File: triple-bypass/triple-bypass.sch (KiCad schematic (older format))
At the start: 65 parts, among them CON101 MD-90SM, J101 HDR1X2, J102 HDR1X3, U101 THS7374IPWR, U102 LMV358M8G-13

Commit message: more parts placement
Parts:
- renumbered SL2 to SR2, XL2 to XR2, YL2 to YR2
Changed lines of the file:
@@
 $EndDescr
 $Comp
-L +5V #PWR01
+L +5V #PWR9
 U 1 1 5A68CA11
 P 9000 1050
-F 0 "#PWR01" H 9000 900 50  0001 C CNN
+F 0 "#PWR9" H 9000 900 50  0001 C CNN
 F 1 "+5V" H 9000 1190 50  0000 C CNN
 F 2 "" H 9000 1050 50  0001 C CNN
@@
 $EndComp
 $Comp
-L GND #PWR02
+L GND #PWR10
 U 1 1 5A68CAEB
 P 9000 2650
-F 0 "#PWR02" H 9000 2400 50  0001 C CNN
+F 0 "#PWR10" H 9000 2400 50  0001 C CNN
 F 1 "GND" H 9000 2500 50  0000 C CNN
 F 2 "" H 9000 2650 50  0001 C CNN
@@
 $EndComp
 $Comp
-L GND #PWR03
+L GND #PWR3
 U 1 1 5A68EF32
 P 2650 2900
-F 0 "#PWR03" H 2650 2650 50  0001 C CNN
+F 0 "#PWR3" H 2650 2650 50  0001 C CNN
 F 1 "GND" H 2650 2750 50  0000 C CNN
 F 2 "" H 2650 2900 50  0001 C CNN
@@
 $EndComp
 $Comp
-L +5V #PWR04
+L +5V #PWR5
 U 1 1 5A68FF2A
 P 3700 2300
-F 0 "#PWR04" H 3700 2150 50  0001 C CNN
+F 0 "#PWR5" H 3700 2150 50  0001 C CNN
 F 1 "+5V" H 3700 2440 50  0000 C CNN
 F 2 "" H 3700 2300 50  0001 C CNN
@@
 $EndComp
 $Comp
-L +5V #PWR05
+L +5V #PWR1
 U 1 1 5A693A27
 P 1650 850
-F 0 "#PWR05" H 1650 700 50  0001 C CNN
+F 0 "#PWR1" H 1650 700 50  0001 C CNN
 F 1 "+5V" H 1650 990 50  0000 C CNN
 F 2 "" H 1650 850 50  0001 C CNN
@@
 CSYNC at video level \nalways drives the CVBS \nsignal because bags of\nmoney from HD Retrovision
 $Comp
-L GND #PWR06
+L GND #PWR8
 U 1 1 5A6ACD1A
 P 8025 6200
-F 0 "#PWR06" H 8025 5950 50  0001 C CNN
+F 0 "#PWR8" H 8025 5950 50  0001 C CNN
 F 1 "GND" H 8025 6050 50  0000 C CNN
 F 2 "" H 8025 6200 50  0001 C CNN
@@
 $EndComp
 $Comp
-L +5V #PWR07
+L +5V #PWR7
 U 1 1 5A6ADA07
 P 8025 5150
-F 0 "#PWR07" H 8025 5000 50  0001 C CNN
+F 0 "#PWR7" H 8025 5000 50  0001 C CNN
 F 1 "+5V" H 8025 5290 50  0000 C CNN
 F 2 "" H 8025 5150 50  0001 C CNN
@@
 $EndComp
 $Comp
-L +5V #PWR08
+L +5V #PWR4
 U 1 1 5A6B0DB3
 P 2975 7275
-F 0 "#PWR08" H 2975 7125 50  0001 C CNN
+F 0 "#PWR4" H 2975 7125 50  0001 C CNN
 F 1 "+5V" H 2975 7415 50  0000 C CNN
 F 2 "" H 2975 7275 50  0001 C CNN
@@
 $EndComp
 $Comp
-L GND #PWR09
+L GND #PWR6
 U 1 1 5A6B0E82
 P 4175 7400
-F 0 "#PWR09" H 4175 7150 50  0001 C CNN
+F 0 "#PWR6" H 4175 7150 50  0001 C CNN
 F 1 "GND" H 4175 7250 50  0000 C CNN
 F 2 "" H 4175 7400 50  0001 C CNN
@@
 $EndComp
 $Comp
-L GND #PWR010
+L GND #PWR2
 U 1 1 5A6C4582
 P 2000 6800
-F 0 "#PWR010" H 2000 6550 50  0001 C CNN
+F 0 "#PWR2" H 2000 6550 50  0001 C CNN
 F 1 "GND" H 2000 6650 50  0000 C CNN
 F 2 "" H 2000 6800 50  0001 C CNN
@@
 Connection ~ 2000 5200
 $Comp
-L TP_50 XL2
+L TP_50 XR2
 U 1 1 5A6CEA61
 P 1150 5600
-F 0 "XL2" H 825 5600 60  0000 C CNN
+F 0 "XR2" H 825 5600 60  0000 C CNN
 F 1 "TP_50" H 1250 5800 60  0001 C CNN
 F 2 "db-smt:TP50" H 1450 5900 60  0001 C CNN
@@
 $EndComp
 $Comp
-L TP_50 SL2
+L TP_50 SR2
 U 1 1 5A6CEB6B
 P 1150 6000
-F 0 "SL2" H 825 6000 60  0000 C CNN
+F 0 "SR2" H 825 6000 60  0000 C CNN
 F 1 "TP_50" H 1250 6200 60  0001 C CNN
 F 2 "db-smt:TP50" H 1450 6300 60  0001 C CNN
@@
 $EndComp
 $Comp
-L TP_50 YL2
+L TP_50 YR2
 U 1 1 5A6CEC64
 P 1150 6400
-F 0 "YL2" H 825 6400 60  0000 C CNN
+F 0 "YR2" H 825 6400 60  0000 C CNN
 F 1 "TP_50" H 1250 6600 60  0001 C CNN
 F 2 "db-smt:TP50" H 1450 6700 60  0001 C CNN

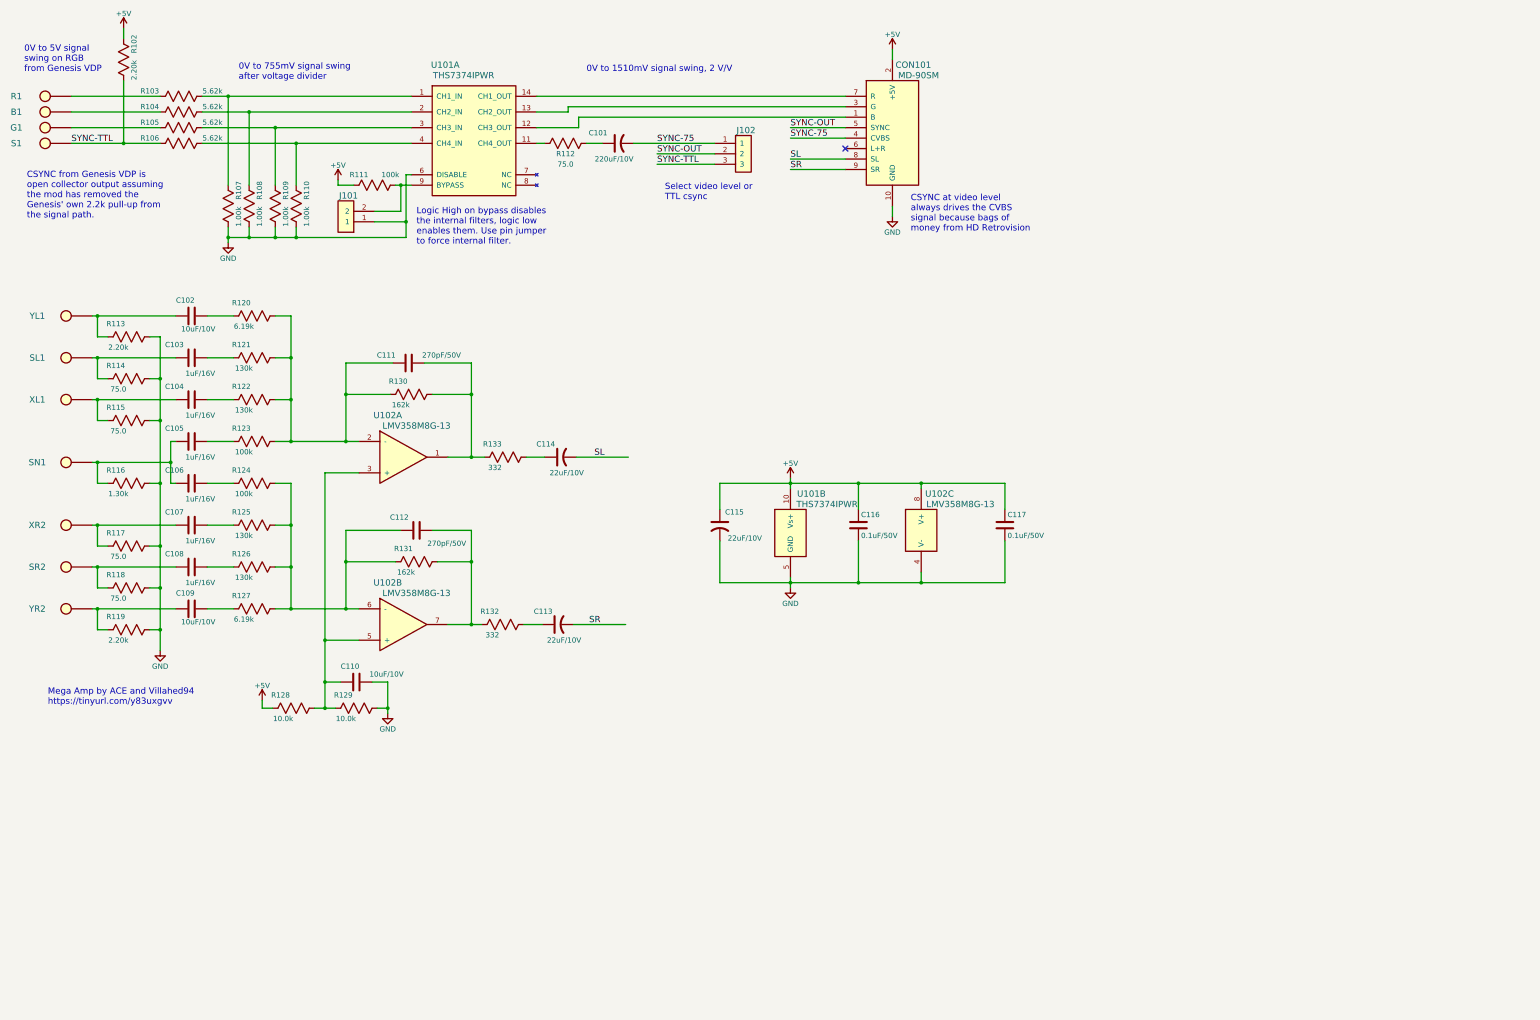
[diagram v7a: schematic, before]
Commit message: v0.3 prelim routing complete, sch added
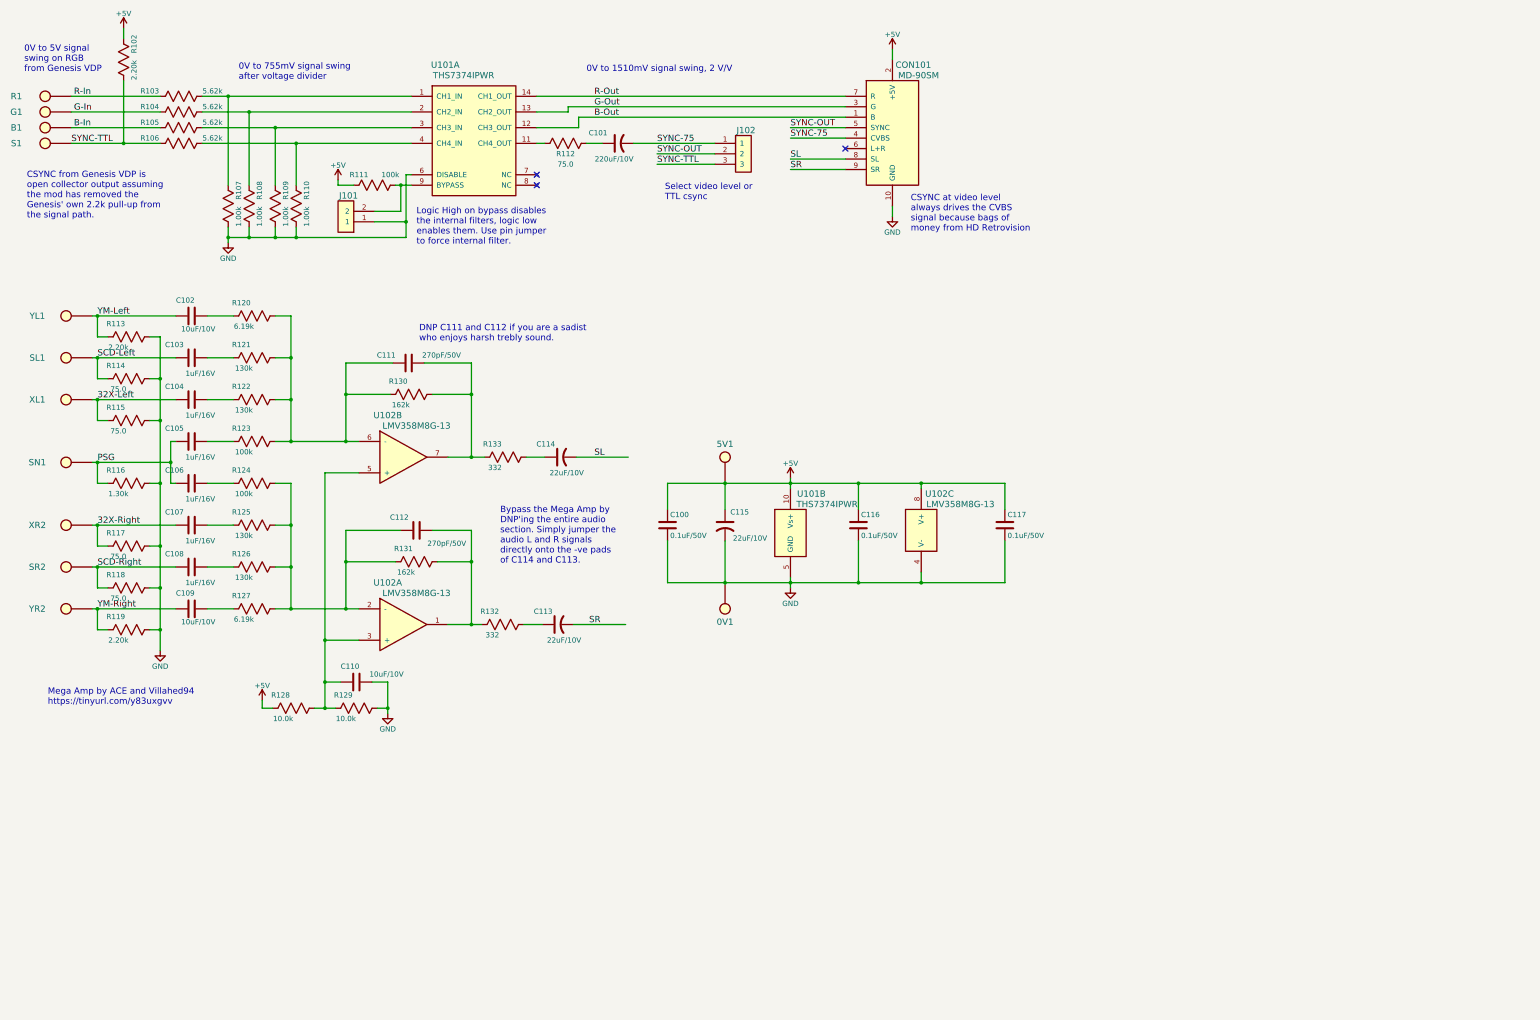
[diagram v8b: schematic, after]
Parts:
- added 0V1, 5V1: TP_50, db-smt:TP50, symbol TP_50
- added C100: 0.1uF/50V, db-smt:0603, symbol C
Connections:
- net +5V: now also 5V1.1, C100.1
- net GND: now also 0V1.1, C100.2
- net B-In: now reaches R105.2
- net B-In: now also B1.1; no longer G1.1
- net G-In: now reaches R104.2
- net G-In: now also G1.1; no longer B1.1
- net R-In: now reaches R1.1, R103.2
- net at C111.2, R130.2, R133.1: now also U102.7 (OUTB); no longer U102.1 (OUTA)
- net at C111.1, R120.2, R121.2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: now also U102.6 (-); no longer U102.2 (-)
- net at C112.1, R124.2, R125.2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: now also U102.2 (-); no longer U102.6 (-)
- net at C112.2, R131.2, R132.1: now also U102.1 (OUTA); no longer U102.7 (OUTB)
- net B-Out: now reaches CON101.1 (B), U101.12 (CH3_OUT)
- net G-Out: now reaches CON101.3 (G), U101.13 (CH2_OUT)
- net R-Out: now reaches CON101.7 (R), U101.14 (CH1_OUT)
- net YM-Left: now reaches C102.2, R113.1, YL1.1
- net SCD-Left: now reaches C103.1, R114.1, SL1.1
- net 32X-Left: now reaches C104.1, R115.1, XL1.1
- net PSG: now reaches C105.1, C106.1, R116.1, SN1.1
- net 32X-Right: now reaches C107.1, R117.1, XR2.1
- net SCD-Right: now reaches C108.1, R118.1, SR2.1
- net YM-Right: now reaches C109.2, R119.1, YR2.1
- no-connect marks 1 -> 3
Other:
- note added: "Bypass the Mega Amp by \nDNP'ing the entire audio \nsection. Simply jumper the\naudio L and R signals \ndirectly onto the -ve pads \nof C114 and C113."
- note added: "DNP C111 and C112 if you are a sadist \nwho enjoys harsh trebly sound."
- moved on the sheet: B1, C115, G1, U102A, U102B
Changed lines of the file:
@@
 Sheet 1 1
 Title "Triple Bypass"
-Date "2018-01-25"
-Rev "0.2"
+Date "2018-08-01"
+Rev "0.3"
 Comp "db Electronics"
 Comment1 "https://github.com/db-electronics/triple-bypass-kicad"
@@
 $EndDescr
 $Comp
-L +5V #PWR9
+L +5V #PWR01
 U 1 1 5A68CA11
 P 9000 1050
-F 0 "#PWR9" H 9000 900 50  0001 C CNN
+F 0 "#PWR01" H 9000 900 50  0001 C CNN
 F 1 "+5V" H 9000 1190 50  0000 C CNN
 F 2 "" H 9000 1050 50  0001 C CNN
@@
 $EndComp
 $Comp
-L GND #PWR10
+L GND #PWR02
 U 1 1 5A68CAEB
 P 9000 2650
-F 0 "#PWR10" H 9000 2400 50  0001 C CNN
+F 0 "#PWR02" H 9000 2400 50  0001 C CNN
 F 1 "GND" H 9000 2500 50  0000 C CNN
 F 2 "" H 9000 2650 50  0001 C CNN
@@
 $EndComp
 $Comp
-L GND #PWR3
+L GND #PWR03
 U 1 1 5A68EF32
 P 2650 2900
-F 0 "#PWR3" H 2650 2650 50  0001 C CNN
+F 0 "#PWR03" H 2650 2650 50  0001 C CNN
 F 1 "GND" H 2650 2750 50  0000 C CNN
 F 2 "" H 2650 2900 50  0001 C CNN
@@
 $EndComp
 $Comp
-L +5V #PWR5
+L +5V #PWR04
 U 1 1 5A68FF2A
 P 3700 2300
-F 0 "#PWR5" H 3700 2150 50  0001 C CNN
+F 0 "#PWR04" H 3700 2150 50  0001 C CNN
 F 1 "+5V" H 3700 2440 50  0000 C CNN
 F 2 "" H 3700 2300 50  0001 C CNN
@@
 $EndComp
 $Comp
-L +5V #PWR1
+L +5V #PWR05
 U 1 1 5A693A27
 P 1650 850
-F 0 "#PWR1" H 1650 700 50  0001 C CNN
+F 0 "#PWR05" H 1650 700 50  0001 C CNN
 F 1 "+5V" H 1650 990 50  0000 C CNN
 F 2 "" H 1650 850 50  0001 C CNN
@@
 L LMV358M8G-13 U102
 U 1 1 5A6950CB
+P 4100 6300
+F 0 "U102" H 4175 6450 60  0000 C CNN
+F 1 "LMV358M8G-13" H 4450 6350 60  0000 C CNN
+F 2 "db-smt:TSSOP-8_3.0mm" H 4375 6825 60  0001 C CNN
+F 3 "https://www.diodes.com/assets/Datasheets/LMV321_358.pdf" H 5200 6750 60  0001 C CNN
+F 4 "LMV358M8G-13DITR-ND" H 4450 6550 60  0001 C CNN "Digikey"
+F 5 "IC OPAMP GP 1MHZ RRO 8MSOP" H 4550 6650 60  0001 C CNN "Description"
+	1    4100 6300
+	1    0    0    -1
+$EndComp
+$Comp
+L LMV358M8G-13 U102
+U 2 1 5A69514A
 P 4100 4700
 F 0 "U102" H 4175 4850 60  0000 C CNN
@@
 F 4 "LMV358M8G-13DITR-ND" H 4450 4950 60  0001 C CNN "Digikey"
 F 5 "IC OPAMP GP 1MHZ RRO 8MSOP" H 4550 5050 60  0001 C CNN "Description"
-	1    4100 4700
-	1    0    0    -1
-$EndComp
-$Comp
-L LMV358M8G-13 U102
-U 2 1 5A69514A
-P 4100 6300
-F 0 "U102" H 4175 6450 60  0000 C CNN
-F 1 "LMV358M8G-13" H 4450 6350 60  0000 C CNN
-F 2 "db-smt:TSSOP-8_3.0mm" H 4375 6825 60  0001 C CNN
-F 3 "https://www.diodes.com/assets/Datasheets/LMV321_358.pdf" H 5200 6750 60  0001 C CNN
-F 4 "LMV358M8G-13DITR-ND" H 4450 6550 60  0001 C CNN "Digikey"
-F 5 "IC OPAMP GP 1MHZ RRO 8MSOP" H 4550 6650 60  0001 C CNN "Description"
-	2    4100 6300
+	2    4100 4700
 	1    0    0    -1
 $EndComp
@@
 CSYNC at video level \nalways drives the CVBS \nsignal because bags of\nmoney from HD Retrovision
 $Comp
-L GND #PWR8
+L GND #PWR06
 U 1 1 5A6ACD1A
 P 8025 6200
-F 0 "#PWR8" H 8025 5950 50  0001 C CNN
+F 0 "#PWR06" H 8025 5950 50  0001 C CNN
 F 1 "GND" H 8025 6050 50  0000 C CNN
 F 2 "" H 8025 6200 50  0001 C CNN
@@
 $EndComp
 $Comp
-L +5V #PWR7
+L +5V #PWR07
 U 1 1 5A6ADA07
 P 8025 5150
-F 0 "#PWR7" H 8025 5000 50  0001 C CNN
+F 0 "#PWR07" H 8025 5000 50  0001 C CNN
 F 1 "+5V" H 8025 5290 50  0000 C CNN
 F 2 "" H 8025 5150 50  0001 C CNN
@@
 L CP_1206 C115
 U 1 1 5A6B1599
-P 7350 5600
-F 0 "C115" H 7400 5725 50  0000 L CNN
-F 1 "22uF/10V" H 7425 5475 50  0000 L CNN
-F 2 "db-smt:1206_P" H 7650 5450 30  0001 C CNN
-F 3 "" H 7480 5650 60  0000 C CNN
-F 4 "478-1663-1-ND" H 7580 5750 60  0001 C CNN "Digikey"
-F 5 "CAP TANT 22UF 10V 10% 1206" H 7575 5850 60  0001 C CNN "Description"
-	1    7350 5600
+P 7400 5600
+F 0 "C115" H 7450 5725 50  0000 L CNN
+F 1 "22uF/10V" H 7475 5475 50  0000 L CNN
+F 2 "db-smt:1206_P" H 7700 5450 30  0001 C CNN
+F 3 "" H 7530 5650 60  0000 C CNN
+F 4 "478-1663-1-ND" H 7630 5750 60  0001 C CNN "Digikey"
+F 5 "CAP TANT 22UF 10V 10% 1206" H 7625 5850 60  0001 C CNN "Description"
+	1    7400 5600
 	1    0    0    -1
 $EndComp
@@
 $EndComp
 $Comp
-L +5V #PWR4
+L +5V #PWR08
 U 1 1 5A6B0DB3
 P 2975 7275
-F 0 "#PWR4" H 2975 7125 50  0001 C CNN
+F 0 "#PWR08" H 2975 7125 50  0001 C CNN
 F 1 "+5V" H 2975 7415 50  0000 C CNN
 F 2 "" H 2975 7275 50  0001 C CNN
@@
 $EndComp
 $Comp
-L GND #PWR6
+L GND #PWR09
 U 1 1 5A6B0E82
 P 4175 7400
-F 0 "#PWR6" H 4175 7150 50  0001 C CNN
+F 0 "#PWR09" H 4175 7150 50  0001 C CNN
 F 1 "GND" H 4175 7250 50  0000 C CNN
 F 2 "" H 4175 7400 50  0001 C CNN
@@
 $EndComp
 $Comp
-L GND #PWR2
+L GND #PWR010
 U 1 1 5A6C4582
 P 2000 6800
-F 0 "#PWR2" H 2000 6550 50  0001 C CNN
+F 0 "#PWR010" H 2000 6550 50  0001 C CNN
 F 1 "GND" H 2000 6650 50  0000 C CNN
 F 2 "" H 2000 6800 50  0001 C CNN
@@
 	8025 6100 8025 6200
 Wire Wire Line
-	7350 6150 10075 6150
+	6850 6150 10075 6150
 Wire Wire Line
 	10075 6150 10075 5750
 Connection ~ 8025 6150
 Wire Wire Line
-	7350 5200 10075 5200
+	6850 5200 10075 5200
 Wire Wire Line
 	10075 5200 10075 5450
@@
 Connection ~ 8675 6150
 Wire Wire Line
-	7350 5450 7350 5200
-Wire Wire Line
-	7350 5750 7350 6150
+	7400 5450 7400 5200
+Wire Wire Line
+	7400 5750 7400 6150
 Wire Wire Line
 	5975 4950 6475 4950
@@
 L TP_50 B1
 U 1 1 5A6C96BB
+P 950 1800
+F 0 "B1" H 625 1800 60  0000 C CNN
+F 1 "TP_50" H 1050 2000 60  0001 C CNN
+F 2 "db-smt:TP50" H 1250 2100 60  0001 C CNN
+F 3 "" H 950 1750 60  0001 C CNN
+F 4 "#ND" H 1100 2100 60  0001 C CNN "Digikey"
+F 5 "0.05\" x 0.05\" SMT Test Point" H 1625 2200 60  0001 C CNN "Description"
+	1    950  1800
+	1    0    0    -1
+$EndComp
+$Comp
+L TP_50 G1
+U 1 1 5A6C9788
 P 950 1650
-F 0 "B1" H 625 1650 60  0000 C CNN
+F 0 "G1" H 625 1650 60  0000 C CNN
 F 1 "TP_50" H 1050 1850 60  0001 C CNN
 F 2 "db-smt:TP50" H 1250 1950 60  0001 C CNN
@@
 F 5 "0.05\" x 0.05\" SMT Test Point" H 1625 2050 60  0001 C CNN "Description"
 	1    950  1650
-	1    0    0    -1
-$EndComp
-$Comp
-L TP_50 G1
-U 1 1 5A6C9788
-P 950 1800
-F 0 "G1" H 625 1800 60  0000 C CNN
-F 1 "TP_50" H 1050 2000 60  0001 C CNN
-F 2 "db-smt:TP50" H 1250 2100 60  0001 C CNN
-F 3 "" H 950 1750 60  0001 C CNN
-F 4 "#ND" H 1100 2100 60  0001 C CNN "Digikey"
-F 5 "0.05\" x 0.05\" SMT Test Point" H 1625 2200 60  0001 C CNN "Description"
-	1    950  1800
 	1    0    0    -1
 $EndComp
@@
 	1    0    0    -1
 $EndComp
+$Comp
+L TP_50 0V1
+U 1 1 5B61AECD
+P 7400 6350
+F 0 "0V1" V 7225 6350 60  0000 C CNN
+F 1 "TP_50" H 7500 6550 60  0001 C CNN
+F 2 "db-smt:TP50" H 7700 6650 60  0001 C CNN
+F 3 "" H 7400 6300 60  0001 C CNN
+F 4 "#ND" H 7550 6650 60  0001 C CNN "Digikey"
+F 5 "0.05\" x 0.05\" SMT Test Point" H 8075 6750 60  0001 C CNN "Description"
+	1    7400 6350
+	0    -1   -1   0
+$EndComp
+$Comp
+L TP_50 5V1
+U 1 1 5B61D47D
+P 7400 5000
+F 0 "5V1" V 7225 5000 60  0000 C CNN
+F 1 "TP_50" H 7500 5200 60  0001 C CNN
+F 2 "db-smt:TP50" H 7700 5300 60  0001 C CNN
+F 3 "" H 7400 4950 60  0001 C CNN
+F 4 "#ND" H 7550 5300 60  0001 C CNN "Digikey"
+F 5 "0.05\" x 0.05\" SMT Test Point" H 8075 5400 60  0001 C CNN "Description"
+	1    7400 5000
+	0    1    1    0
+$EndComp
+$Comp
+L C C100
+U 1 1 5B620D60
+P 6850 5600
+F 0 "C100" H 6875 5700 50  0000 L CNN
+F 1 "0.1uF/50V" H 6875 5500 50  0000 L CNN
+F 2 "db-smt:0603" H 6888 5450 30  0001 C CNN
+F 3 "" H 6850 5600 60  0000 C CNN
+F 4 "445-5666-1-ND" H 6850 5600 60  0001 C CNN "Digikey"
+F 5 "CAP CER 0.1UF 50V X7R 0603" H 6850 5600 60  0001 C CNN "Description"
+	1    6850 5600
+	1    0    0    -1
+$EndComp
+Wire Wire Line
+	6850 5200 6850 5450
+Connection ~ 7400 5200
+Wire Wire Line
+	6850 6150 6850 5750
+Connection ~ 7400 6150
+Text Label 1400 3600 0    60   ~ 0
+YM-Left
+Text Label 1400 4000 0    60   ~ 0
+SCD-Left
+Text Label 1400 4400 0    60   ~ 0
+32X-Left
+Text Label 1400 5000 0    60   ~ 0
+PSG
+Text Label 1400 5600 0    60   ~ 0
+32X-Right
+Text Label 1400 6000 0    60   ~ 0
+SCD-Right
+Text Label 1400 6400 0    60   ~ 0
+YM-Right
+Text Label 6150 1500 0    60   ~ 0
+R-Out
+Text Label 6150 1600 0    60   ~ 0
+G-Out
+Text Label 6150 1700 0    60   ~ 0
+B-Out
+Text Label 1175 1500 0    60   ~ 0
+R-In
+Text Label 1175 1650 0    60   ~ 0
+G-In
+Text Label 1175 1800 0    60   ~ 0
+B-In
+Text Notes 4475 3850 0    60   ~ 0
+DNP C111 and C112 if you are a sadist \nwho enjoys harsh trebly sound.
+Text Notes 5250 5975 0    60   ~ 0
+Bypass the Mega Amp by \nDNP'ing the entire audio \nsection. Simply jumper the\naudio L and R signals \ndirectly onto the -ve pads \nof C114 and C113.
+NoConn ~ 5600 2250
+NoConn ~ 5600 2350
 $EndSCHEMATC
